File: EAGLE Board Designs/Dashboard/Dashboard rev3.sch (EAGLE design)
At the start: 91 parts, among them J2 CONNECTOR-8_NF_S_RA_BLACK, J3 CONNECTOR-CAN_NF_S_RA_BLACK, J4 CONNECTOR-AVR-ISP_2X05_SMD_, K1 CPC1002N, Q1 TRANSISTOR_N_MOS__PMV15ENEA, Q2 TRANSISTOR_N_MOS__PMV15ENEA, Q3 TRANSISTOR_N_MOS__PMV15ENEA, Q4 TRANSISTOR_N_MOS__PMV15ENEA, Q5 TRANSISTOR_N_MOS__PMV15ENEA, Q6 TRANSISTOR_N_MOS__PMV15ENEA, U1 ATMEGA328P-AU, U2 TCAN1051HQV-Q1, U3 MCP2515, U4 MCP23S17, U5 CONVERTER_DC/DC_12V-5V, U6 RE46C100, X1 CRYSTAL16MHZ, X2 CRYSTAL16MHZ, X7 CONNECTOR-8NANO-FIT_RIGHT_ANG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

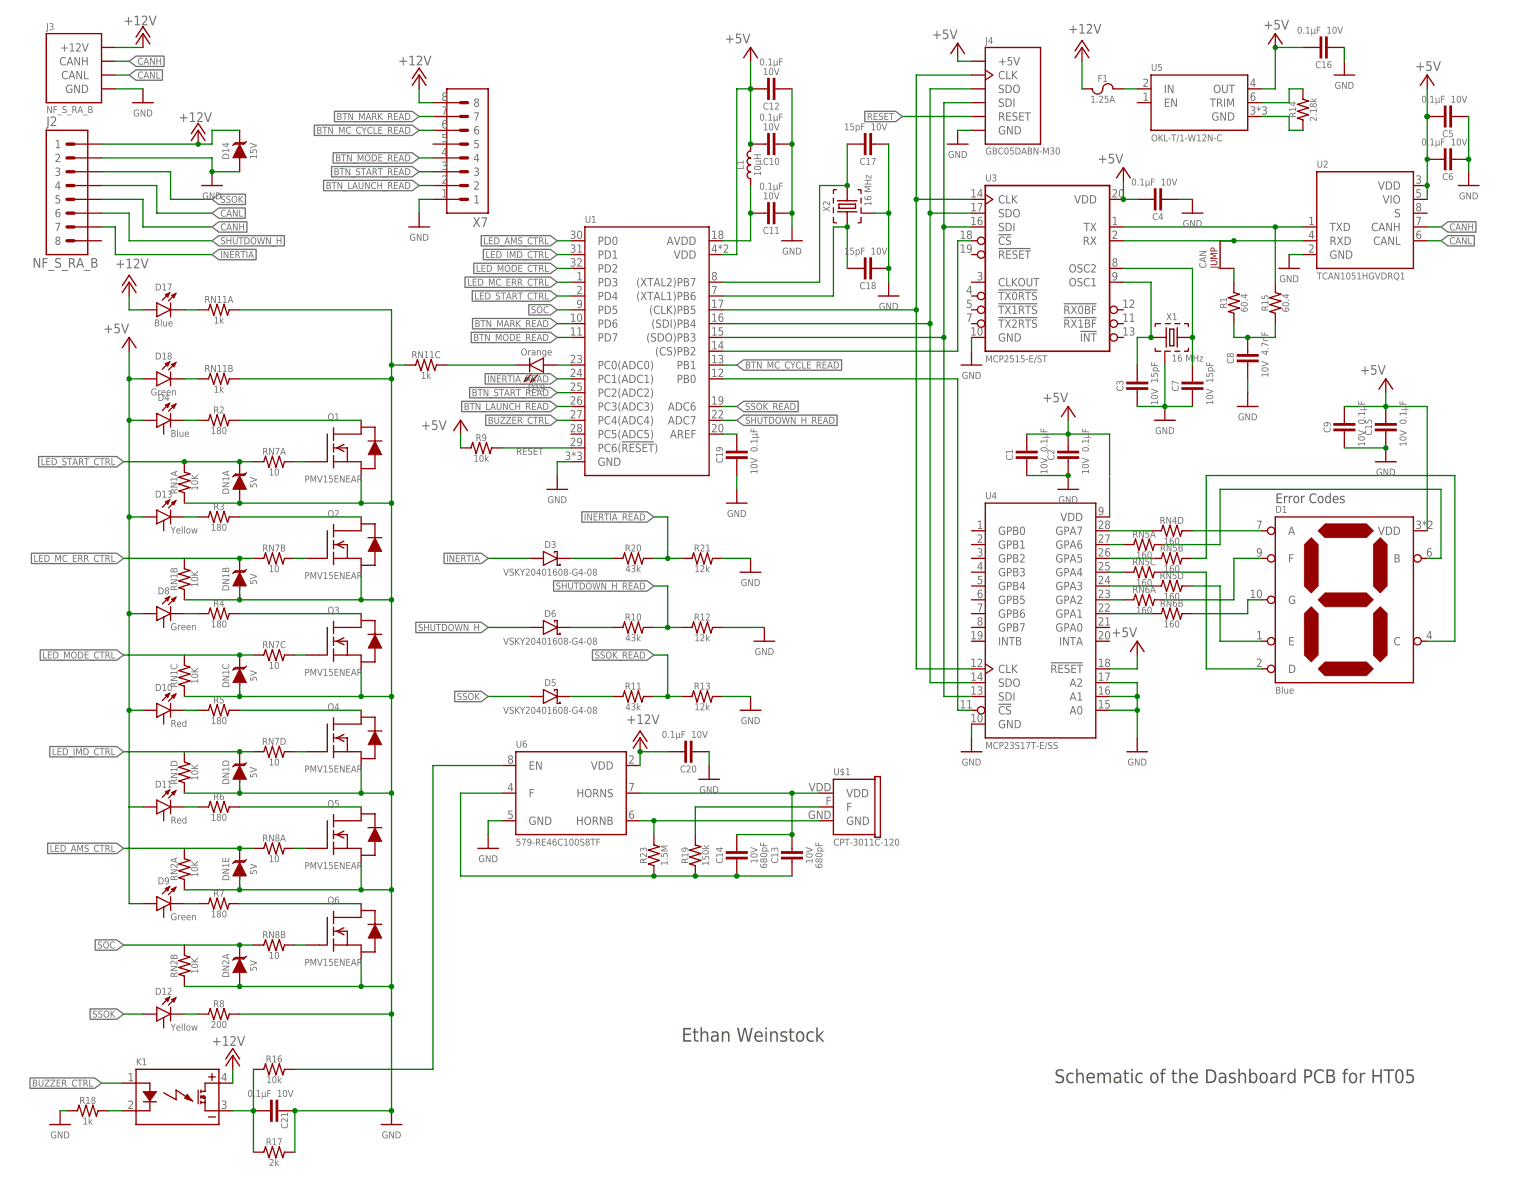
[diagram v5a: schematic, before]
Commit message: Fixed couple warnings for ERC
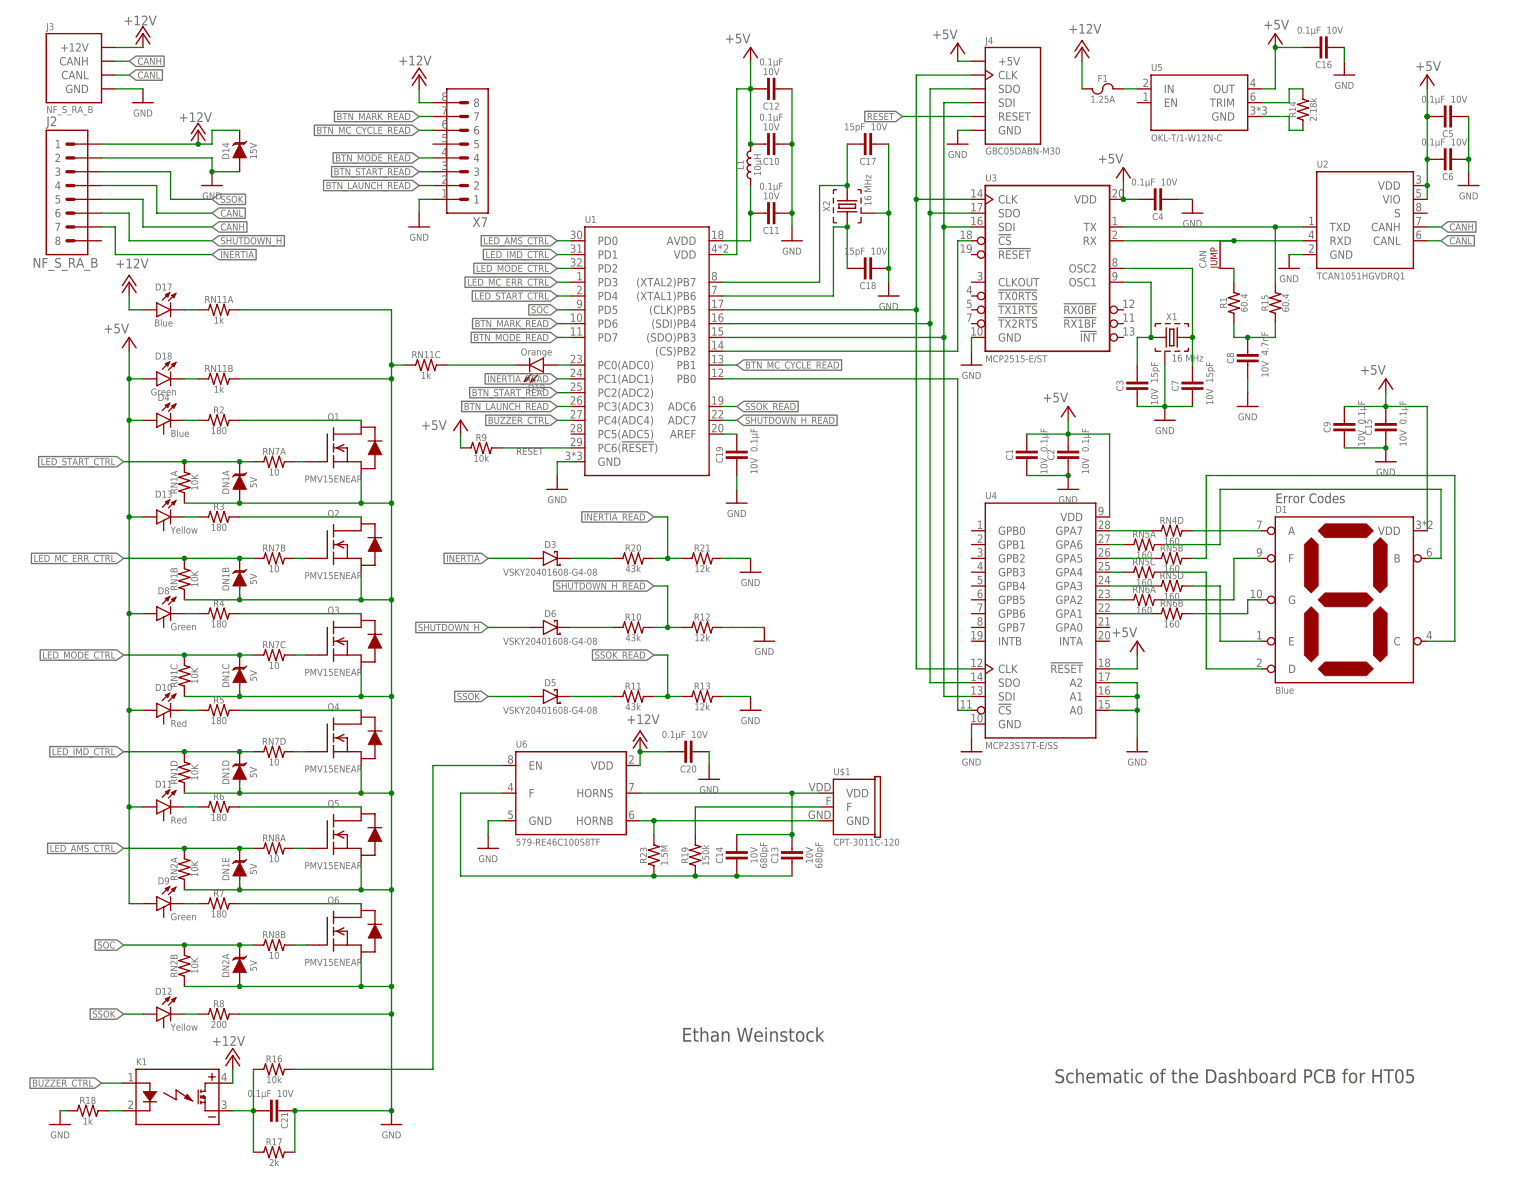
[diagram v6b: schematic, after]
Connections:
- net +5V: now also U4.VDD
- net N$21: now also D3.A; no longer U4.VDD
- net SSOK: no longer D3.A
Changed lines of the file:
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@@
 <pinref part="C2" gate="G$1" pin="1"/>
 <wire x1="205.74" y1="134.62" x2="198.12" y2="134.62" width="0.1524" layer="91"/>
-<wire x1="205.74" y1="127" x2="205.74" y2="134.62" width="0.1524" layer="91"/>
+<pinref part="U4" gate="G$1" pin="VDD"/>
+<wire x1="205.74" y1="134.62" x2="205.74" y2="119.38" width="0.1524" layer="91"/>
 </segment>
 </net>
@@
 <pinref part="J2" gate="G$1" pin="3"/>
 </segment>
-<segment>
-<wire x1="99.06" y1="111.76" x2="91.44" y2="111.76" width="0.1524" layer="91"/>
-<pinref part="D3" gate="G$1" pin="A"/>
-</segment>
 </net>
 <net name="BUZZER_OUT" class="0">
@@
 <label x="24.384" y="111.76" size="1.27" layer="95" rot="R180" xref="yes"/>
 <pinref part="RN1" gate="B" pin="2"/>
+<wire x1="24.384" y1="111.76" x2="35.56" y2="111.76" width="0.1524" layer="91"/>
+<pinref part="DN1" gate="B" pin="C"/>
+<pinref part="RN7" gate="B" pin="1"/>
+<wire x1="48.26" y1="111.76" x2="45.72" y2="111.76" width="0.1524" layer="91"/>
 <wire x1="45.72" y1="111.76" x2="35.56" y2="111.76" width="0.1524" layer="91"/>
-<pinref part="DN1" gate="B" pin="C"/>
 <junction x="45.72" y="111.76"/>
-<wire x1="24.384" y1="111.76" x2="35.56" y2="111.76" width="0.1524" layer="91"/>
-<wire x1="48.26" y1="111.76" x2="45.72" y2="111.76" width="0.1524" layer="91"/>
-<pinref part="RN7" gate="B" pin="1"/>
+<junction x="35.56" y="111.76"/>
 </segment>
 </net>
@@
 <label x="24.384" y="93.98" size="1.27" layer="95" rot="R180" xref="yes"/>
 <pinref part="RN1" gate="C" pin="2"/>
-<wire x1="35.56" y1="93.98" x2="45.72" y2="93.98" width="0.1524" layer="91"/>
+<wire x1="24.384" y1="93.98" x2="35.56" y2="93.98" width="0.1524" layer="91"/>
+<pinref part="RN7" gate="C" pin="1"/>
 <pinref part="DN1" gate="C" pin="C"/>
+<wire x1="45.72" y1="93.98" x2="48.26" y2="93.98" width="0.1524" layer="91"/>
+<wire x1="45.72" y1="93.98" x2="35.56" y2="93.98" width="0.1524" layer="91"/>
 <junction x="45.72" y="93.98"/>
-<wire x1="24.384" y1="93.98" x2="35.56" y2="93.98" width="0.1524" layer="91"/>
-<wire x1="45.72" y1="93.98" x2="48.26" y2="93.98" width="0.1524" layer="91"/>
-<pinref part="RN7" gate="C" pin="1"/>
+<junction x="35.56" y="93.98"/>
 </segment>
 </net>
@@
 <label x="24.384" y="76.2" size="1.27" layer="95" rot="R180" xref="yes"/>
 <pinref part="RN1" gate="D" pin="2"/>
-<wire x1="35.56" y1="76.2" x2="45.72" y2="76.2" width="0.1524" layer="91"/>
+<wire x1="24.384" y1="76.2" x2="35.56" y2="76.2" width="0.1524" layer="91"/>
+<pinref part="RN7" gate="D" pin="1"/>
 <pinref part="DN1" gate="D" pin="C"/>
+<wire x1="45.72" y1="76.2" x2="48.26" y2="76.2" width="0.1524" layer="91"/>
+<wire x1="45.72" y1="76.2" x2="35.56" y2="76.2" width="0.1524" layer="91"/>
 <junction x="45.72" y="76.2"/>
-<wire x1="24.384" y1="76.2" x2="35.56" y2="76.2" width="0.1524" layer="91"/>
-<wire x1="45.72" y1="76.2" x2="48.26" y2="76.2" width="0.1524" layer="91"/>
-<pinref part="RN7" gate="D" pin="1"/>
+<junction x="35.56" y="76.2"/>
 </segment>
 </net>
@@
 <label x="24.384" y="58.42" size="1.27" layer="95" rot="R180" xref="yes"/>
 <pinref part="RN2" gate="A" pin="2"/>
-<wire x1="35.56" y1="58.42" x2="45.72" y2="58.42" width="0.1524" layer="91"/>
+<wire x1="24.384" y1="58.42" x2="35.56" y2="58.42" width="0.1524" layer="91"/>
+<pinref part="RN8" gate="A" pin="1"/>
 <pinref part="DN1" gate="E" pin="C"/>
+<wire x1="45.72" y1="58.42" x2="48.26" y2="58.42" width="0.1524" layer="91"/>
+<wire x1="45.72" y1="58.42" x2="35.56" y2="58.42" width="0.1524" layer="91"/>
 <junction x="45.72" y="58.42"/>
-<wire x1="24.384" y1="58.42" x2="35.56" y2="58.42" width="0.1524" layer="91"/>
-<wire x1="45.72" y1="58.42" x2="48.26" y2="58.42" width="0.1524" layer="91"/>
-<pinref part="RN8" gate="A" pin="1"/>
+<junction x="35.56" y="58.42"/>
 </segment>
 </net>
@@
 <net name="+5V1" class="0">
 <segment>
+<wire x1="27.94" y1="48.26" x2="25.4" y2="48.26" width="0.1524" layer="91"/>
 <wire x1="25.4" y1="48.26" x2="25.4" y2="66.04" width="0.1524" layer="91"/>
-<wire x1="27.94" y1="48.26" x2="25.4" y2="48.26" width="0.1524" layer="91"/>
 <wire x1="25.4" y1="66.04" x2="25.4" y2="83.82" width="0.1524" layer="91"/>
 <wire x1="25.4" y1="83.82" x2="25.4" y2="101.6" width="0.1524" layer="91"/>
@@
 <wire x1="27.94" y1="83.82" x2="25.4" y2="83.82" width="0.1524" layer="91"/>
 <junction x="25.4" y="83.82"/>
-<wire x1="27.94" y1="66.04" x2="25.4" y2="66.04" width="0.1524" layer="91"/>
 <wire x1="27.94" y1="137.16" x2="25.4" y2="137.16" width="0.1524" layer="91"/>
 <junction x="25.4" y="137.16"/>
@@
 <pinref part="D9" gate="G$1" pin="A"/>
 <pinref part="D10" gate="G$1" pin="A"/>
-<pinref part="D11" gate="G$1" pin="A"/>
 <wire x1="25.4" y1="144.78" x2="27.94" y2="144.78" width="0.1524" layer="91"/>
 <junction x="25.4" y="144.78"/>
 <pinref part="D18" gate="LED" pin="A"/>
 <pinref part="D13" gate="G$1" pin="A"/>
+<pinref part="D11" gate="G$1" pin="A"/>
+<wire x1="27.94" y1="66.04" x2="25.4" y2="66.04" width="0.1524" layer="91"/>
+<junction x="25.4" y="66.04"/>
 </segment>
 </net>
@@
 <label x="24.384" y="40.64" size="1.27" layer="95" rot="R180" xref="yes"/>
 <pinref part="RN2" gate="B" pin="2"/>
-<wire x1="35.56" y1="40.64" x2="45.72" y2="40.64" width="0.1524" layer="91"/>
+<wire x1="24.384" y1="40.64" x2="35.56" y2="40.64" width="0.1524" layer="91"/>
+<pinref part="RN8" gate="B" pin="1"/>
 <pinref part="DN2" gate="A" pin="C"/>
+<wire x1="45.72" y1="40.64" x2="48.26" y2="40.64" width="0.1524" layer="91"/>
+<wire x1="45.72" y1="40.64" x2="35.56" y2="40.64" width="0.1524" layer="91"/>
 <junction x="45.72" y="40.64"/>
-<wire x1="24.384" y1="40.64" x2="35.56" y2="40.64" width="0.1524" layer="91"/>
-<wire x1="45.72" y1="40.64" x2="48.26" y2="40.64" width="0.1524" layer="91"/>
-<pinref part="RN8" gate="B" pin="1"/>
+<junction x="35.56" y="40.64"/>
 </segment>
 <segment>
@@
 <wire x1="223.52" y1="109.22" x2="223.52" y2="91.44" width="0.1524" layer="91"/>
 <wire x1="223.52" y1="91.44" x2="233.68" y2="91.44" width="0.1524" layer="91"/>
-</segment>
-</net>
-<net name="N$21" class="0">
-<segment>
-<pinref part="U4" gate="G$1" pin="VDD"/>
-<wire x1="205.74" y1="119.38" x2="205.74" y2="126.746" width="0.1524" layer="91"/>
 </segment>
 </net>
@@
 </segment>
 </net>
+<net name="N$21" class="0">
+<segment>
+<pinref part="D3" gate="G$1" pin="A"/>
+<wire x1="91.44" y1="111.76" x2="99.06" y2="111.76" width="0.1524" layer="91"/>
+</segment>
+</net>
